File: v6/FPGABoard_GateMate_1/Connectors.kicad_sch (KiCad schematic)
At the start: 21 parts, among them IC1 TXB0108RUKR, IC2 TXB0108RUKR, IC3 TXB0108RUKR, IC4 TXB0108RUKR, J3 Conn_02x16_Odd_Even, J4 Conn_02x16_Odd_Even, J5 Conn_02x16_Odd_Even, J6 Conn_02x04_Odd_Even, J7 Conn_02x04_Odd_Even

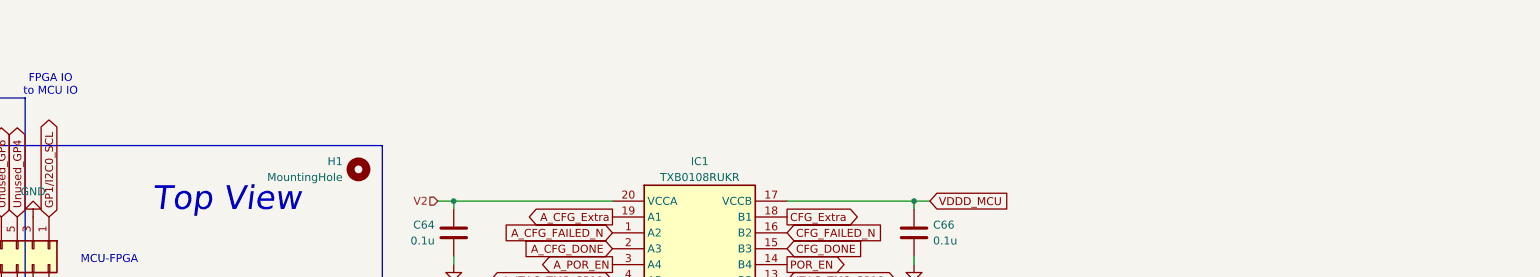
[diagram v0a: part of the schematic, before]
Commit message: Add comments for GateMAte board
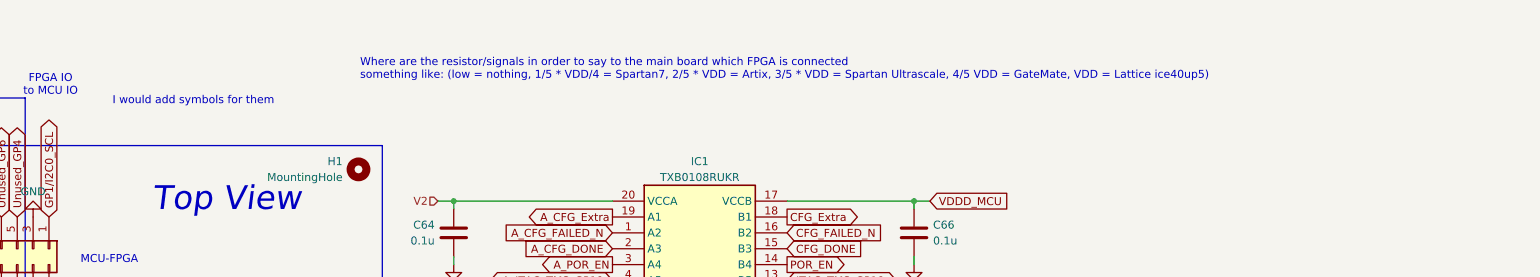
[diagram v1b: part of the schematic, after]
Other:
- note added: "I would add symbols for them"
- note added: "Where are the resistor/signals in order to say to the main board which FPGA is connected something like: (low = nothing, 1/5 * VDD/4 = Spartan7, 2/5 * VDD = Artix, 3/5 * VDD = Spartan Ultrascale, 4/5 VDD = GateMate, VDD = Lattice ice40up5)"
